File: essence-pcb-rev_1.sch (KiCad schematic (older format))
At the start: 1 part

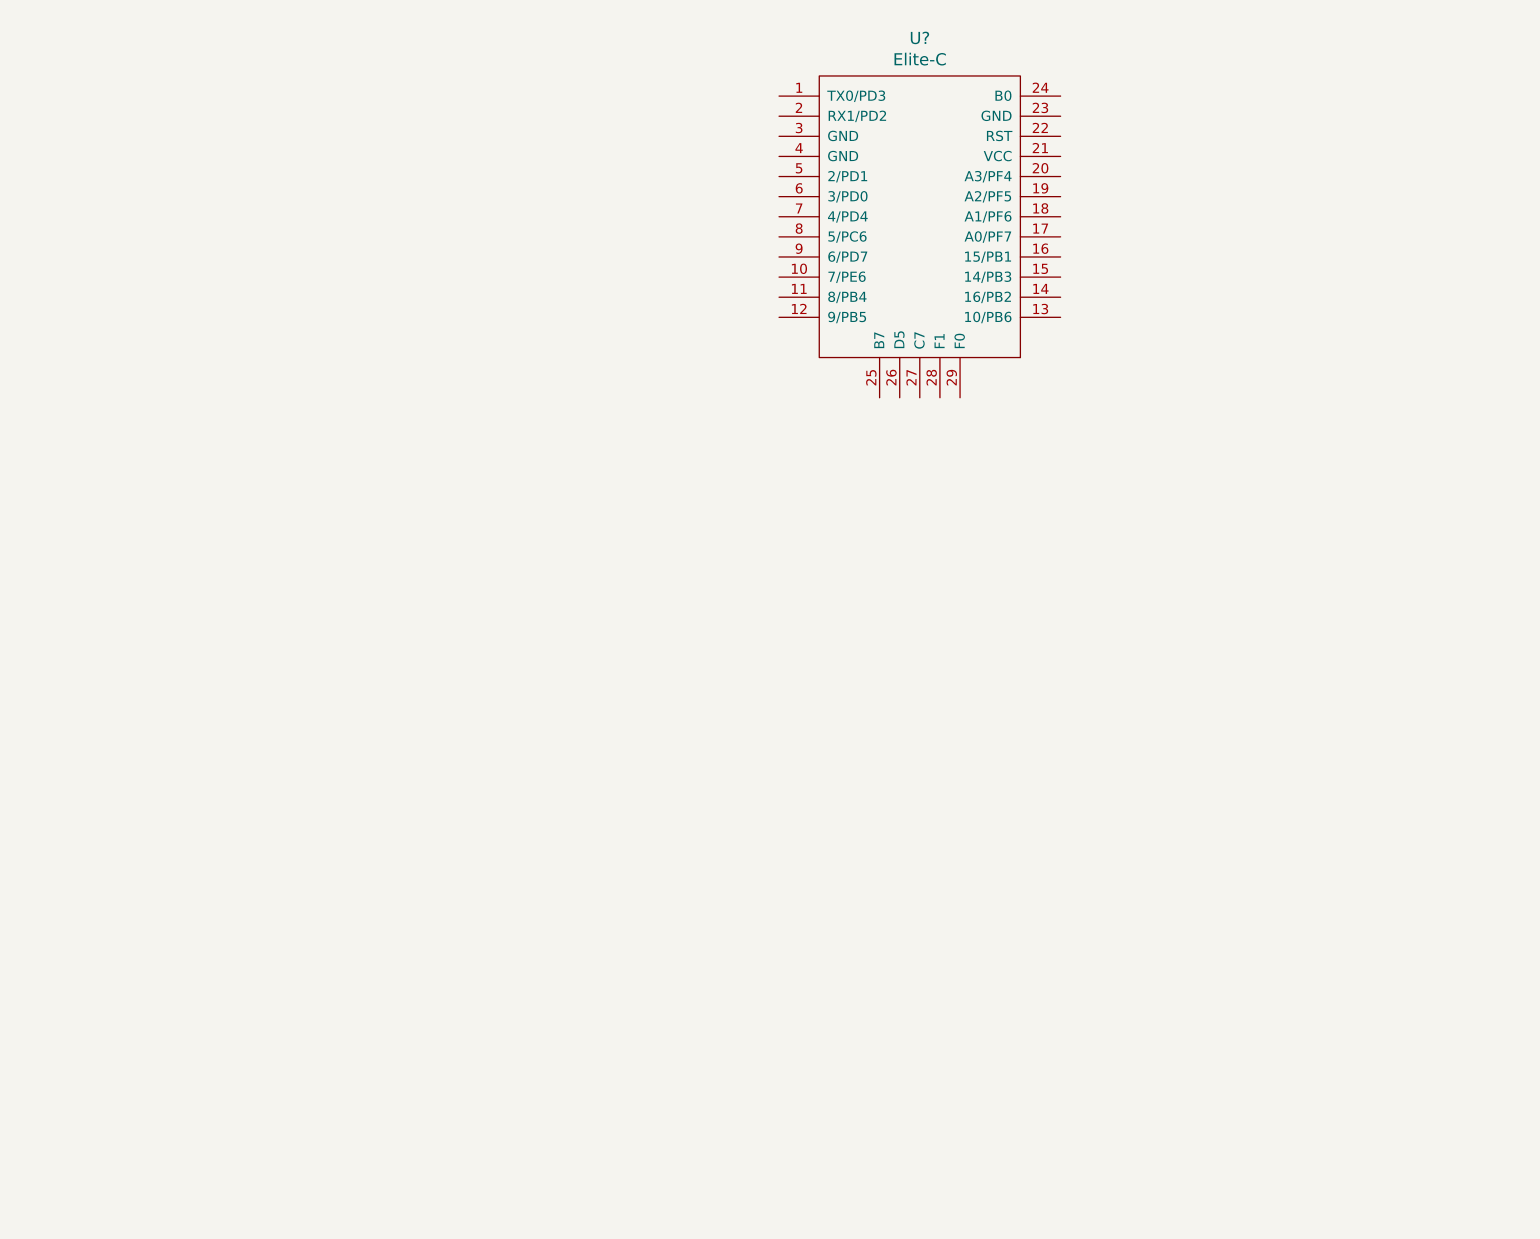
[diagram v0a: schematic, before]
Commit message: Schematic layout
I think I did this right using the Elite-C footprint, but I do not know. Good thing PCBs are cheap to make...kind of
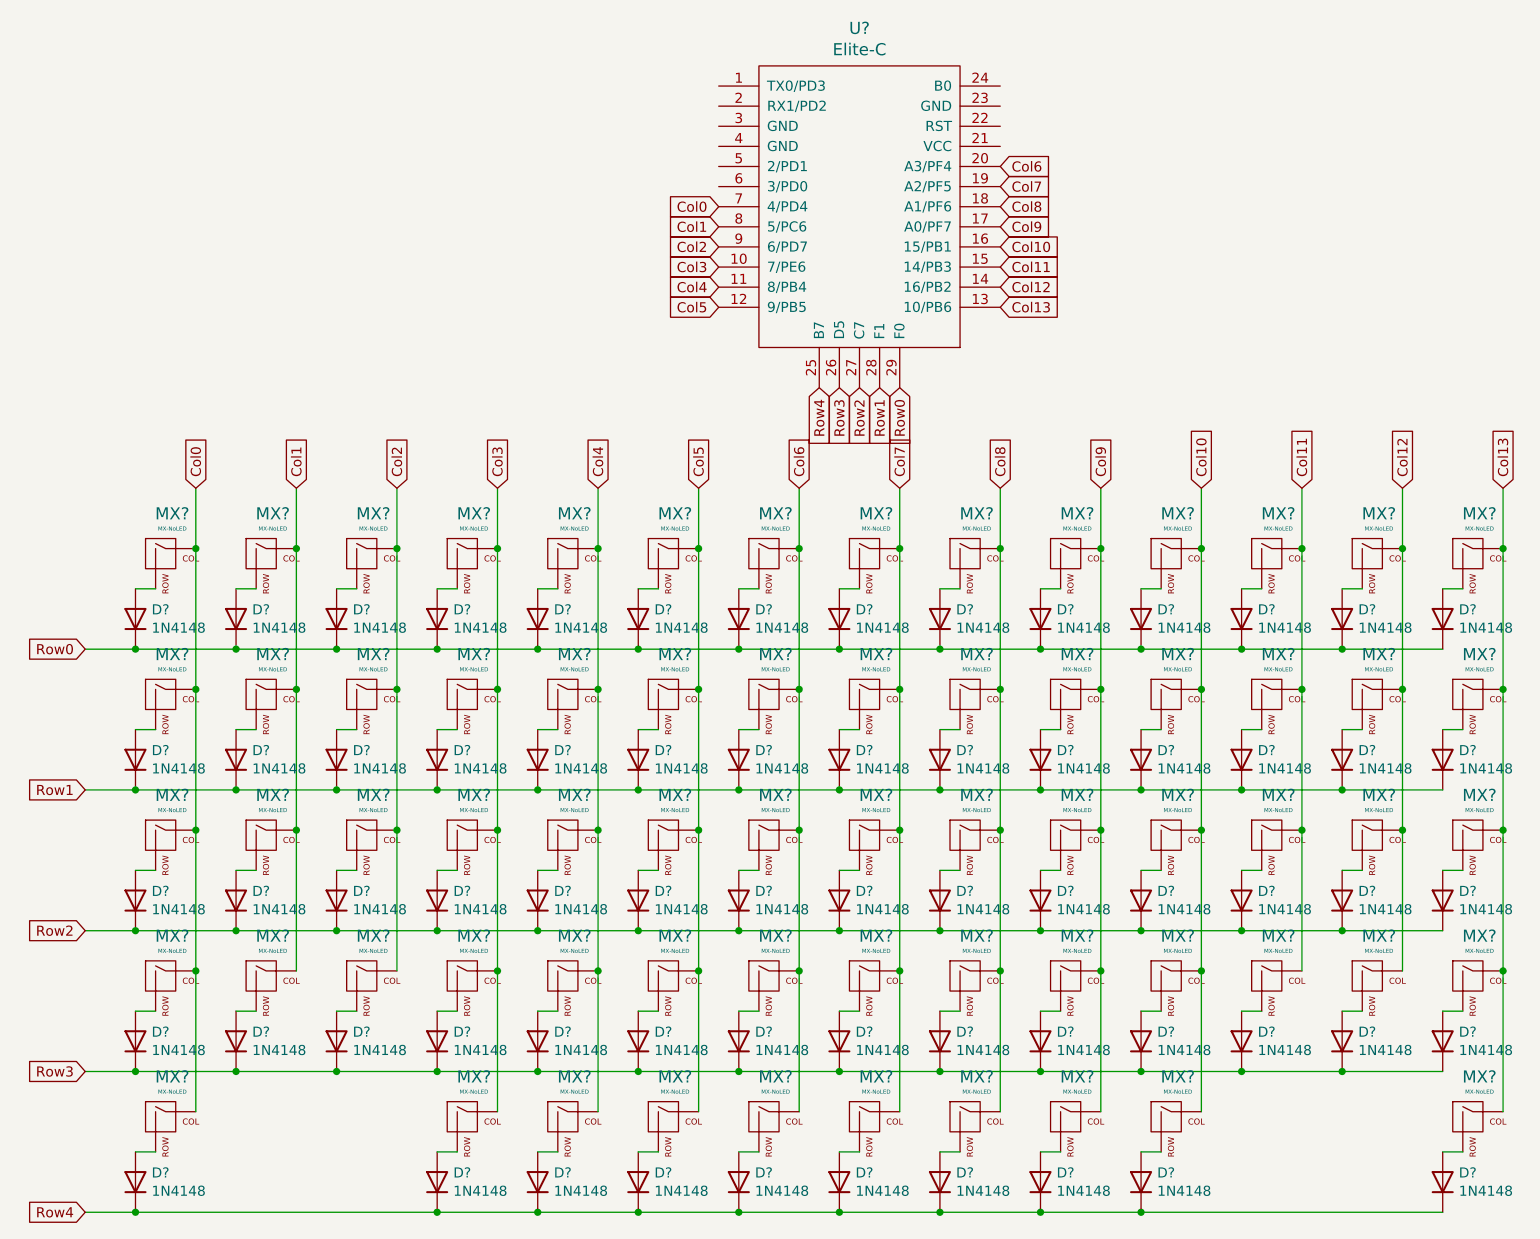
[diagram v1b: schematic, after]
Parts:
- added D? (x66): 1N4148, Diode_THT:D_DO-35_SOD27_P7.62mm_Horizontal, symbol Diode:1N4148
- added MX? (x66): MX-NoLED, symbol MX_Alps_Hybrid:MX-NoLED
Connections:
- net Col3: now reaches U?.10 (7/PE6)
- net Col3: now also MX?.1 (COL), MX?.1 (COL), MX?.1 (COL), MX?.1 (COL), MX?.1 (COL)
- net Col4: now reaches U?.11 (8/PB4)
- net Col4: now also MX?.1 (COL), MX?.1 (COL), MX?.1 (COL), MX?.1 (COL), MX?.1 (COL)
- net Col5: now reaches U?.12 (9/PB5)
- net Col5: now also MX?.1 (COL), MX?.1 (COL), MX?.1 (COL), MX?.1 (COL), MX?.1 (COL)
- net Col13: now reaches U?.13 (10/PB6)
- net Col13: now also MX?.1 (COL), MX?.1 (COL), MX?.1 (COL), MX?.1 (COL), MX?.1 (COL)
- net Col12: now reaches U?.14 (16/PB2)
- net Col12: now also MX?.1 (COL), MX?.1 (COL), MX?.1 (COL), MX?.1 (COL)
- net Col11: now reaches U?.15 (14/PB3)
- net Col11: now also MX?.1 (COL), MX?.1 (COL), MX?.1 (COL), MX?.1 (COL)
- net Col10: now reaches U?.16 (15/PB1)
- net Col10: now also MX?.1 (COL), MX?.1 (COL), MX?.1 (COL), MX?.1 (COL), MX?.1 (COL)
- net Col9: now reaches U?.17 (A0/PF7)
- net Col9: now also MX?.1 (COL), MX?.1 (COL), MX?.1 (COL), MX?.1 (COL), MX?.1 (COL)
- net Col8: now reaches U?.18 (A1/PF6)
- net Col8: now also MX?.1 (COL), MX?.1 (COL), MX?.1 (COL), MX?.1 (COL), MX?.1 (COL)
- net Col7: now reaches U?.19 (A2/PF5)
- net Col7: now also MX?.1 (COL), MX?.1 (COL), MX?.1 (COL), MX?.1 (COL), MX?.1 (COL)
- net Col6: now reaches U?.20 (A3/PF4)
- net Col6: now also MX?.1 (COL), MX?.1 (COL), MX?.1 (COL), MX?.1 (COL), MX?.1 (COL)
- net Row4: now reaches U?.25 (B7)
- net Row4: now also D?.1 (K), D?.1 (K), D?.1 (K), D?.1 (K), D?.1 (K), D?.1 (K), D?.1 (K), D?.1 (K), D?.1 (K), D?.1 (K)
- net Row3: now reaches U?.26 (D5)
- net Row3: now also D?.1 (K), D?.1 (K), D?.1 (K), D?.1 (K), D?.1 (K), D?.1 (K), D?.1 (K), D?.1 (K), D?.1 (K), D?.1 (K), D?.1 (K), D?.1 (K), D?.1 (K), D?.1 (K)
- net Row2: now reaches U?.27 (C7)
- net Row2: now also D?.1 (K), D?.1 (K), D?.1 (K), D?.1 (K), D?.1 (K), D?.1 (K), D?.1 (K), D?.1 (K), D?.1 (K), D?.1 (K), D?.1 (K), D?.1 (K), D?.1 (K), D?.1 (K)
- net Row1: now reaches U?.28 (F1)
- net Row1: now also D?.1 (K), D?.1 (K), D?.1 (K), D?.1 (K), D?.1 (K), D?.1 (K), D?.1 (K), D?.1 (K), D?.1 (K), D?.1 (K), D?.1 (K), D?.1 (K), D?.1 (K), D?.1 (K)
- net Row0: now reaches U?.29 (F0)
- net Row0: now also D?.1 (K), D?.1 (K), D?.1 (K), D?.1 (K), D?.1 (K), D?.1 (K), D?.1 (K), D?.1 (K), D?.1 (K), D?.1 (K), D?.1 (K), D?.1 (K), D?.1 (K), D?.1 (K)
- net Col0: now reaches U?.7 (4/PD4)
- net Col0: now also MX?.1 (COL), MX?.1 (COL), MX?.1 (COL), MX?.1 (COL), MX?.1 (COL)
- net Col1: now reaches U?.8 (5/PC6)
- net Col1: now also MX?.1 (COL), MX?.1 (COL), MX?.1 (COL), MX?.1 (COL)
- net Col2: now reaches U?.9 (6/PD7)
- net Col2: now also MX?.1 (COL), MX?.1 (COL), MX?.1 (COL), MX?.1 (COL)
- new net: D?.2 (A), MX?.2 (ROW) (x66)
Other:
- moved on the sheet: U?

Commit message: Annotations for schematic components
I now need to look for a footprint for the Rotary Encoder, although I think I found it off of the KiCad Subreddit. If you are reading this for some reason, random person, go make a sandwich.
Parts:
- removed D? (x2): 1N4148, Diode_THT:D_DO-35_SOD27_P7.62mm_Horizontal, symbol Diode:1N4148
- removed MX? (x2): MX-NoLED, symbol MX_Alps_Hybrid:MX-NoLED
- gave numbers to parts that had none: 129
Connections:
- net Row3: no longer D64.1 (K), D74.1 (K)
- net Row4: now also D64.1 (K), D74.1 (K)
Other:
- moved on the sheet: D64, D74, MX-64, MX-74

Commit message: Found Rotary Encoder symbol
Why was this so damn difficult to find in KiCad's default libraries? The world may never know...
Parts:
- added SW?: Rotary_Encoder_Switch, symbol Device:Rotary_Encoder_Switch
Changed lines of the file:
@@
 	5500 5950 5500 4550
 Connection ~ 5500 4550
+$Comp
+L Device:Rotary_Encoder_Switch SW?
+U 1 1 6214EE47
+P 7550 1650
+F 0 "SW?" H 7550 2017 50  0000 C CNN
+F 1 "Rotary_Encoder_Switch" H 7550 1926 50  0000 C CNN
+F 2 "" H 7400 1810 50  0001 C CNN
+F 3 "~" H 7550 1910 50  0001 C CNN
+	1    7550 1650
+	1    0    0    -1
+$EndComp
 $EndSCHEMATC

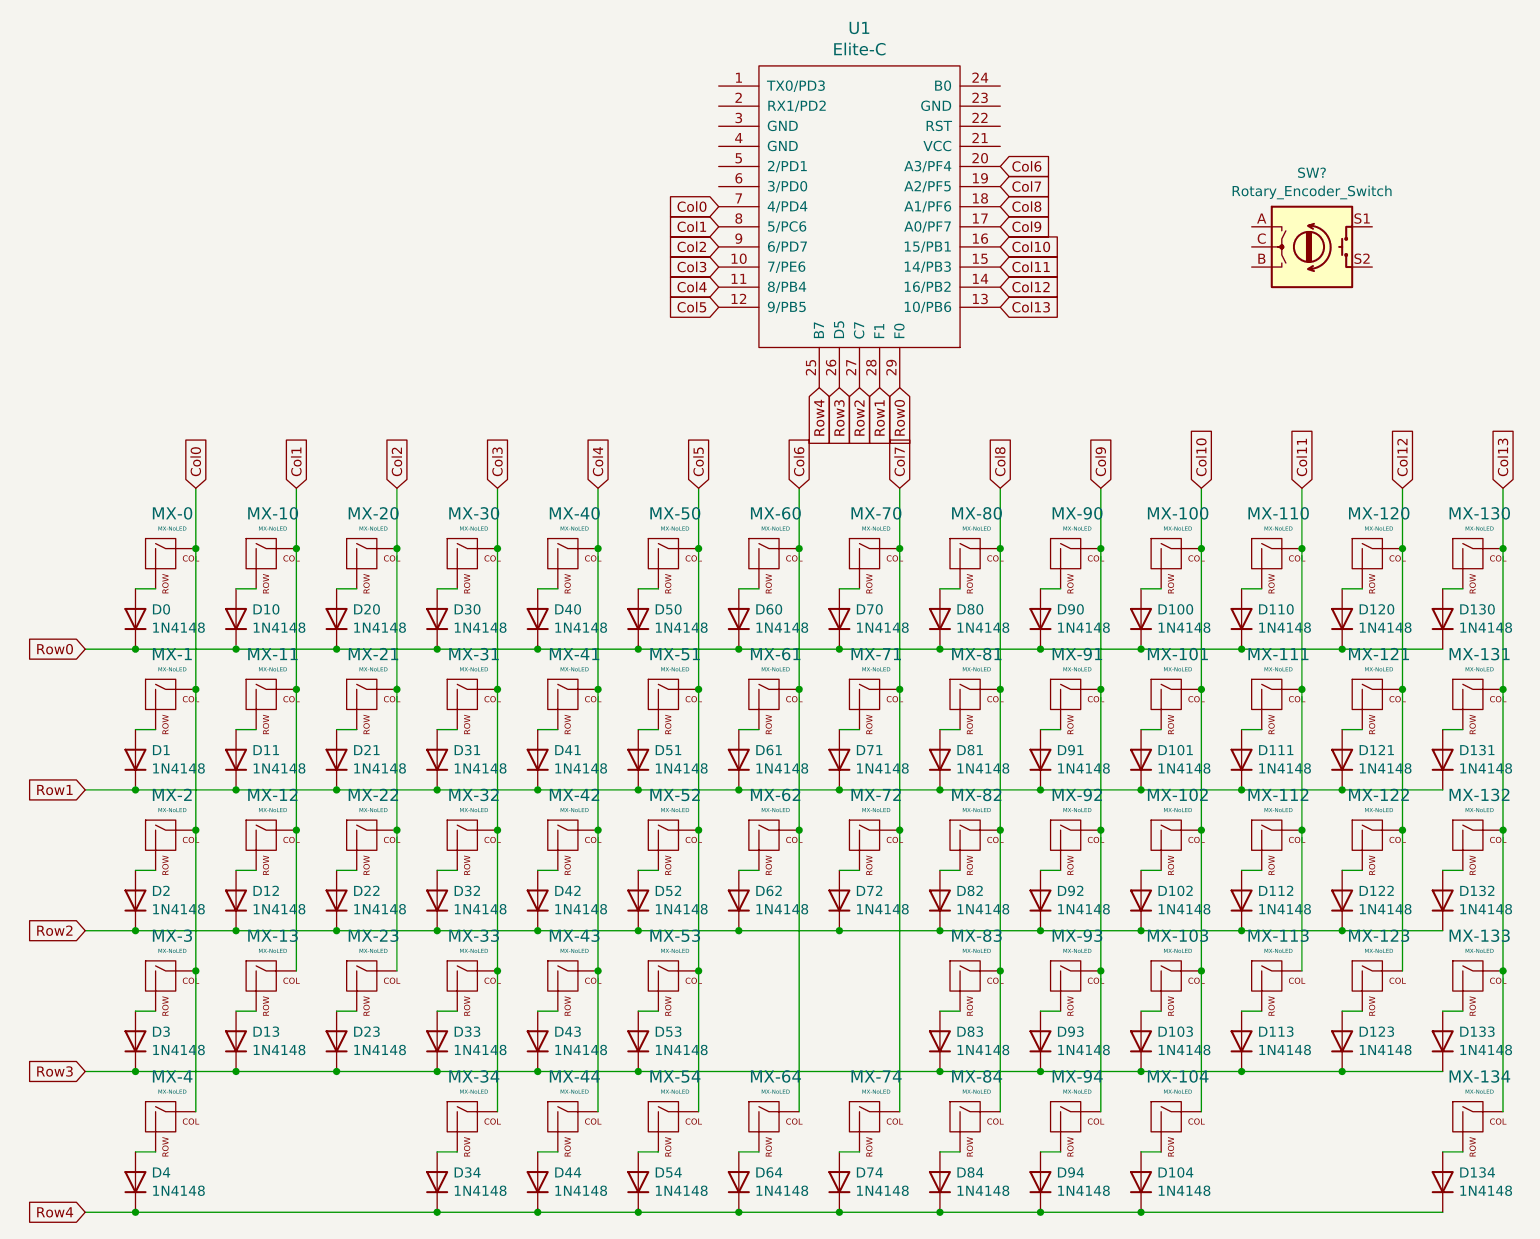
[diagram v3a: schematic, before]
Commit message: Rotary Encoder Slotted into Schematic
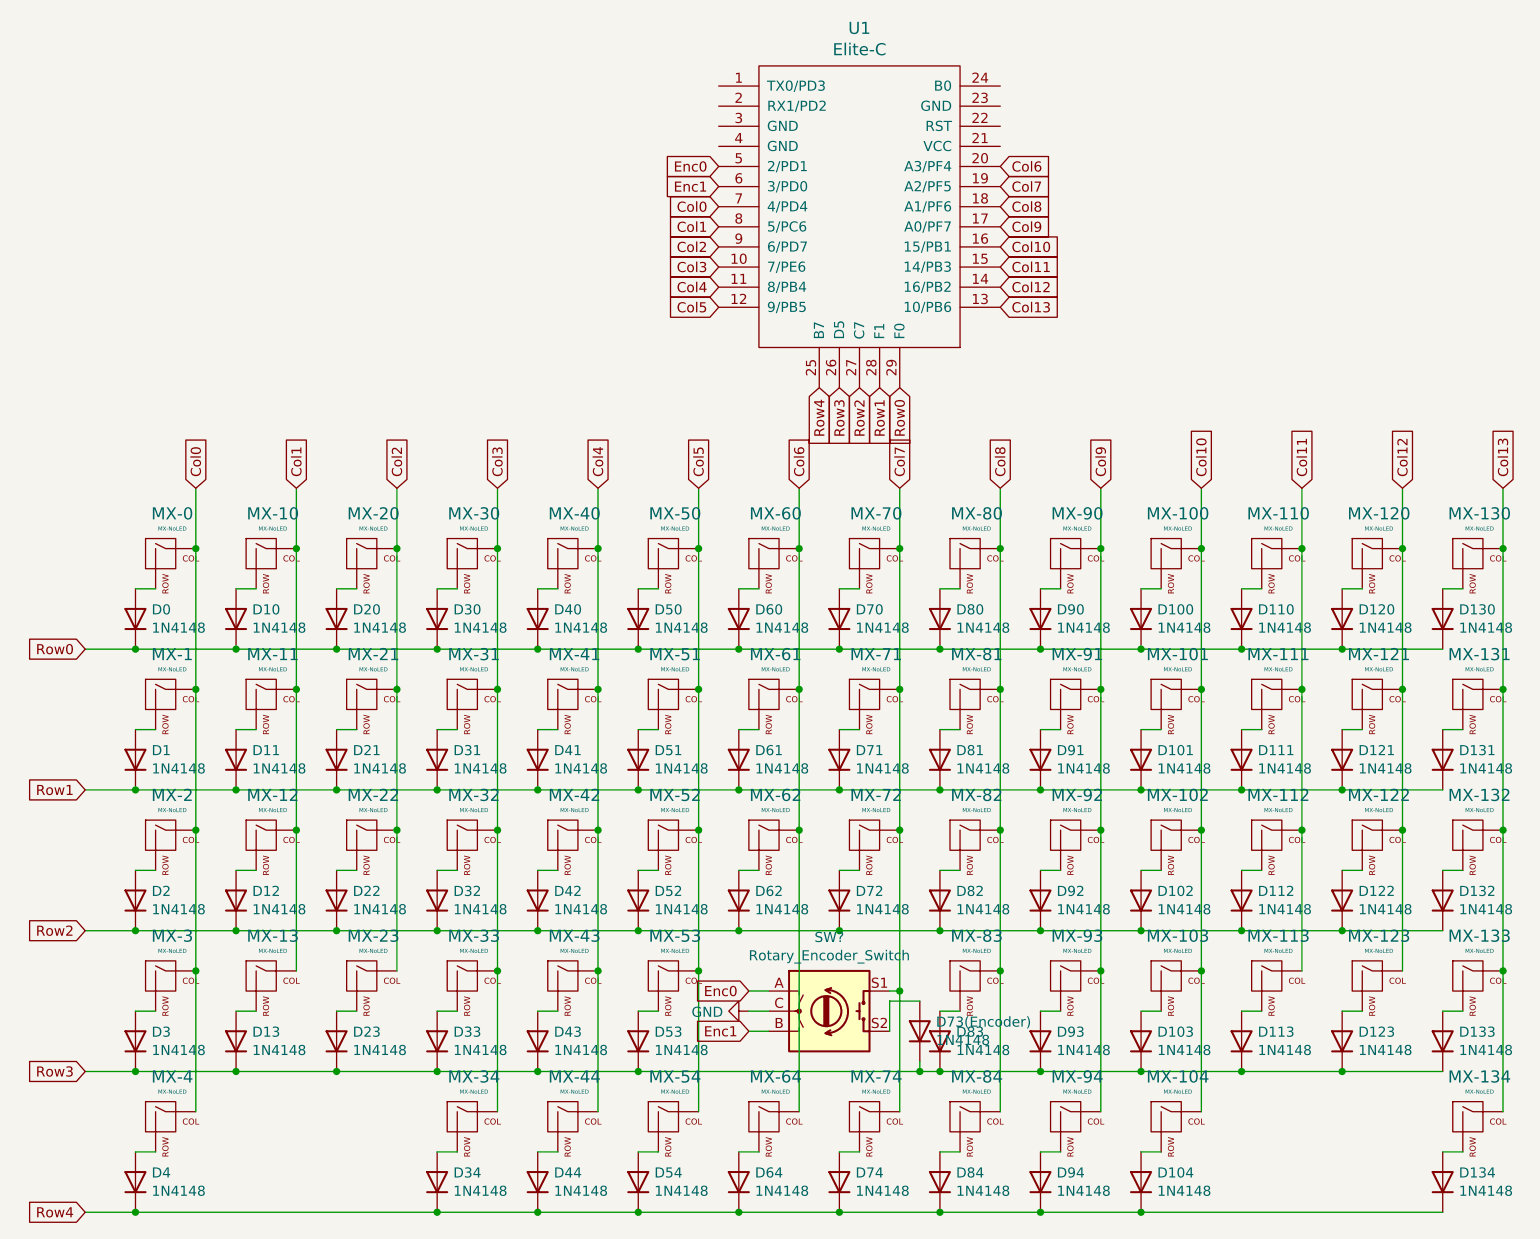
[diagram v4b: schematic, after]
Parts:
- added D73(Encoder): 1N4148, Diode_THT:D_DO-35_SOD27_P7.62mm_Horizontal, symbol Diode:1N4148
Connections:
- net Col7: now also SW?.S1
- net Row3: now also D73(Encoder).1 (K)
- net Enc0: now reaches U1.5 (2/PD1)
- net Enc0: now also SW?.A
- net Enc1: now reaches U1.6 (3/PD0)
- net Enc1: now also SW?.B
- net GND: now reaches SW?.C
- net at SW?.S2: now also D73(Encoder).2 (A)
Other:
- moved on the sheet: SW?
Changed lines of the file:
@@
 Connection ~ 4200 6450
 Wire Wire Line
-	5700 5750 4200 5750
+	5700 5750 5600 5750
 Connection ~ 5700 5750
 Connection ~ 4200 5750
@@
 	5000 5950 5000 4550
 Connection ~ 5000 4550
-Wire Wire Line
-	5500 5950 5500 4550
-Connection ~ 5500 4550
 $Comp
 L Device:Rotary_Encoder_Switch SW?
 U 1 1 6214EE47
-P 7550 1650
-F 0 "SW?" H 7550 2017 50  0000 C CNN
-F 1 "Rotary_Encoder_Switch" H 7550 1926 50  0000 C CNN
-F 2 "" H 7400 1810 50  0001 C CNN
-F 3 "~" H 7550 1910 50  0001 C CNN
-	1    7550 1650
+P 5150 5450
+F 0 "SW?" H 5150 5817 50  0000 C CNN
+F 1 "Rotary_Encoder_Switch" H 5150 5726 50  0000 C CNN
+F 2 "" H 5000 5610 50  0001 C CNN
+F 3 "~" H 5150 5710 50  0001 C CNN
+	1    5150 5450
 	1    0    0    -1
 $EndComp
+Wire Wire Line
+	5500 5950 5500 5350
+Wire Wire Line
+	5500 5350 5450 5350
+Wire Wire Line
+	5500 5350 5500 4550
+Connection ~ 5500 5350
+Connection ~ 5500 4550
+$Comp
+L Diode:1N4148 D73(Encoder)
+U 1 1 6218BDEF
+P 5600 5550
+F 0 "D73(Encoder)" V 5646 5470 50  0000 R CNN
+F 1 "1N4148" V 5555 5470 50  0000 R CNN
+F 2 "Diode_THT:D_DO-35_SOD27_P7.62mm_Horizontal" H 5600 5375 50  0001 C CNN
+F 3 "https://assets.nexperia.com/documents/data-sheet/1N4148_1N4448.pdf" H 5600 5550 50  0001 C CNN
+	1    5600 5550
+	0    -1   -1   0
+$EndComp
+Wire Wire Line
+	5450 5550 5450 5400
+Wire Wire Line
+	5450 5400 5600 5400
+Wire Wire Line
+	5600 5700 5600 5750
+Connection ~ 5600 5750
+Wire Wire Line
+	5600 5750 4200 5750
+$Comp
+L power:GND #PWR?
+U 1 1 621C76ED
+P 4750 5450
+F 0 "#PWR?" H 4750 5200 50  0001 C CNN
+F 1 "GND" V 4755 5322 50  0000 R CNN
+F 2 "" H 4750 5450 50  0001 C CNN
+F 3 "" H 4750 5450 50  0001 C CNN
+	1    4750 5450
+	0    1    1    0
+$EndComp
+Wire Wire Line
+	4850 5450 4750 5450
+Text GLabel 4600 1250 0    50   Input ~ 0
+Enc0
+Text GLabel 4600 1350 0    50   Input ~ 0
+Enc1
+Text GLabel 4750 5350 0    50   Input ~ 0
+Enc0
+Text GLabel 4750 5550 0    50   Input ~ 0
+Enc1
+Wire Wire Line
+	4850 5350 4750 5350
+Wire Wire Line
+	4850 5550 4750 5550
 $EndSCHEMATC
